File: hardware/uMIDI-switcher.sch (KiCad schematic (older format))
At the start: 23 parts, among them U1 MC7809CD, U2 MC7809CD, U3 MC7809CD, U4 MC7809CD, X1 CONN_01X02, X14 uMIDI GPIO3, X16 uMIDI Power, X2 CONN_01X02, X3 CONN_01X02, X4 CONN_01X02

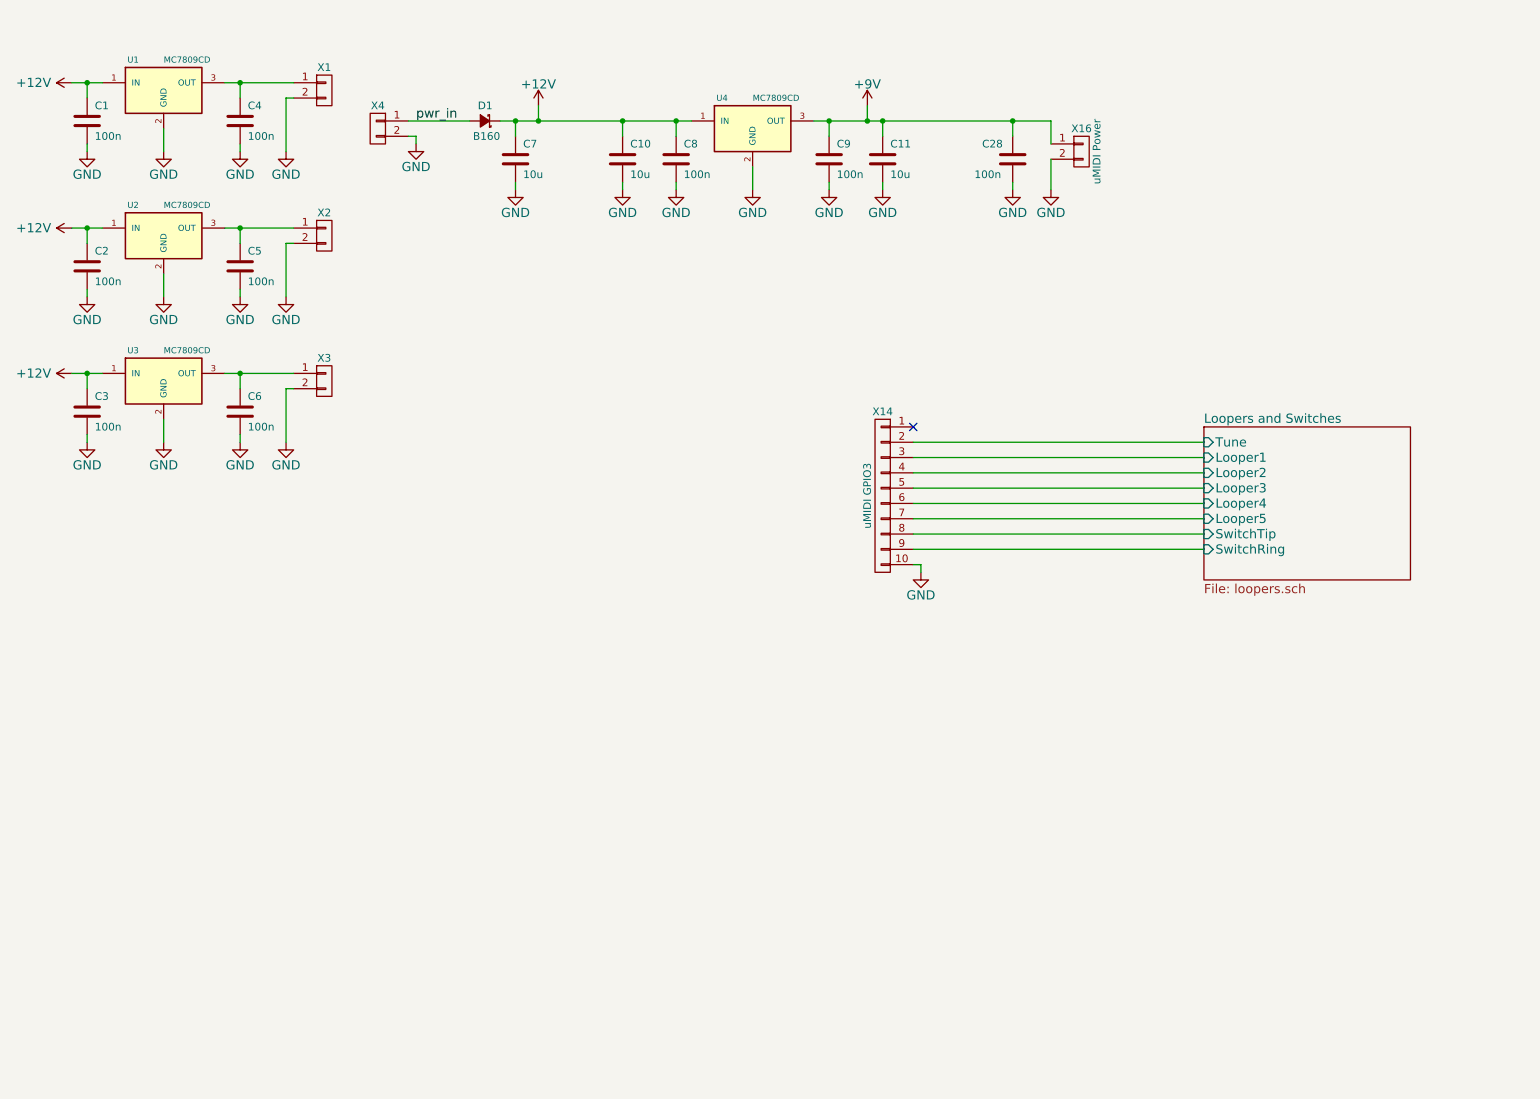
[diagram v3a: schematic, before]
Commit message: Integrate sheet looper.sch into top level sheet
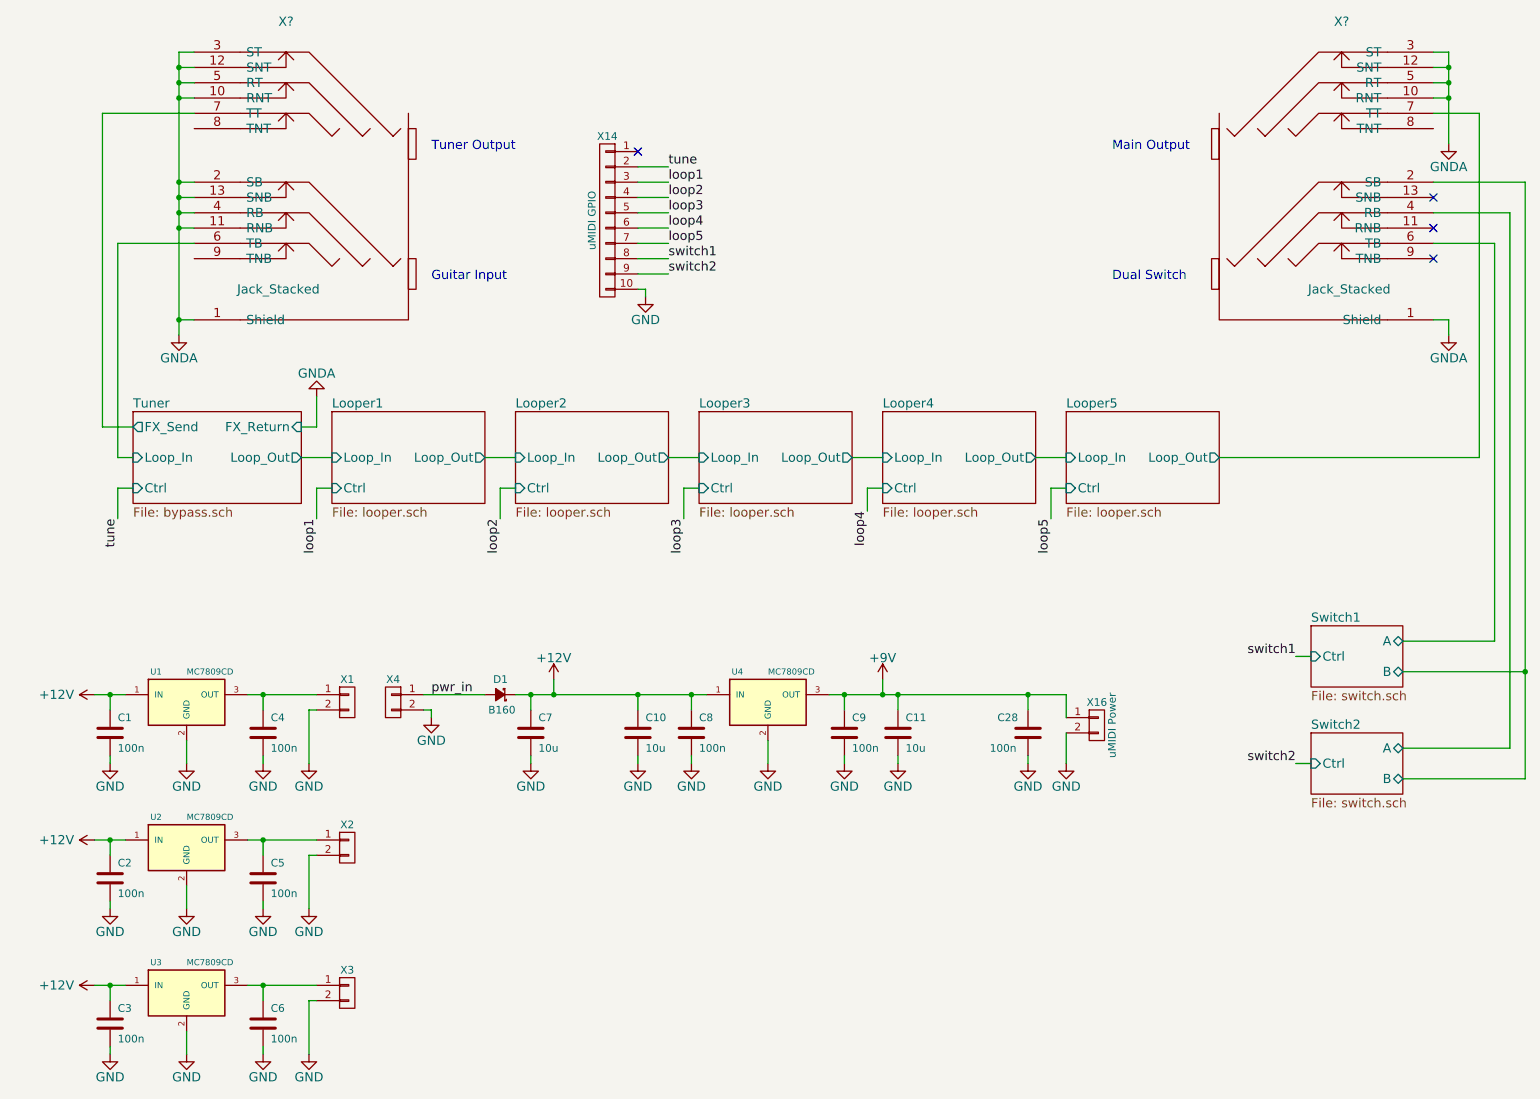
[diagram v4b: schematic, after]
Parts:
- added X? (x2): Jack_Stacked, uMIDI-switcher:NSJ12HF-1, symbol Jack_Stacked
- X14: value uMIDI GPIO3 -> uMIDI GPIO
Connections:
- net Loopers and Switches/Looper1 renamed loop1
- net Loopers and Switches/Looper2 renamed loop2
- net Loopers and Switches/Looper3 renamed loop3
- net Loopers and Switches/Looper4 renamed loop4
- net Loopers and Switches/Looper5 renamed loop5
- net Loopers and Switches/SwitchRing renamed switch2
- net Loopers and Switches/SwitchTip renamed switch1
- net Loopers and Switches/Tune renamed tune
- new net GNDA: X?.1 (Shield), X?.1 (Shield), X?.10 (RNT), X?.10 (RNT), X?.11 (RNB), X?.12 (SNT), X?.12 (SNT), X?.13 (SNB), X?.2 (SB), X?.3 (ST), X?.3 (ST), X?.4 (RB), X?.5 (RT), X?.5 (RT)
- new net Looper5/Loop_Out: X?.7 (TT)
- new net Switch1/A: X?.6 (TB)
- new net Switch1/B: X?.2 (SB)
- new net Switch2/A: X?.4 (RB)
- new net Tuner/FX_Send: X?.7 (TT)
- new net Tuner/Loop_In: X?.6 (TB)
- no-connect marks 1 -> 4
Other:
- note added: "Dual Switch"
- note added: "Guitar Input"
- note added: "Main Output"
- note added: "Tuner Output"
- moved on the sheet: C1, C10, C11, C2, C28, C3, C4, C5, C6, C7, C8, C9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

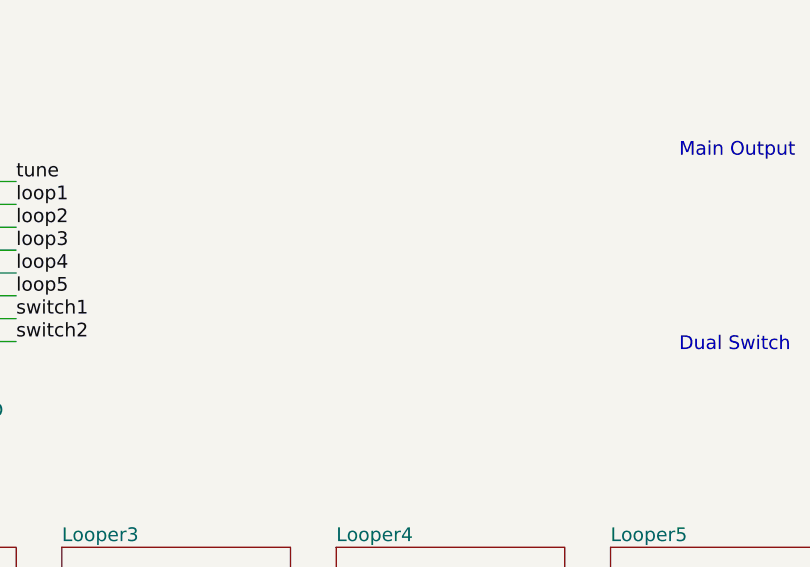
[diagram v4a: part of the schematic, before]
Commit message: Add optional gnd-gnda resistor
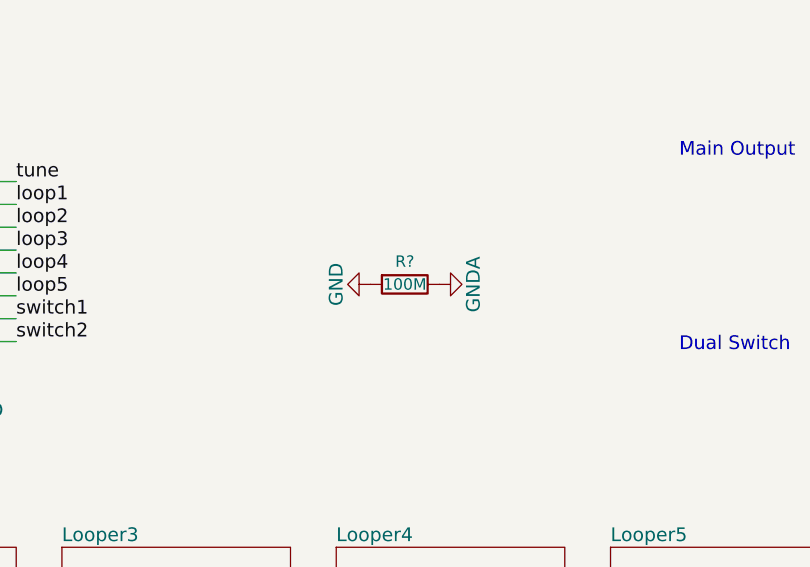
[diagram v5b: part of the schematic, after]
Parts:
- added R?: 100M, Resistors_SMD:R_0603, symbol R
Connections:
- net GND: now also R?.2
- net GNDA: now also R?.1
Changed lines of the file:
@@
 Wire Wire Line
 	4550 2300 4750 2300
+$Comp
+L GNDA #PWR?
+U 1 1 56216618
+P 6600 2050
+F 0 "#PWR?" H 6600 1800 60  0001 C CNN
+F 1 "GNDA" H 6600 1900 60  0000 C CNN
+F 2 "" H 6600 2050 60  0000 C CNN
+F 3 "" H 6600 2050 60  0000 C CNN
+	1    6600 2050
+	0    -1   -1   0
+$EndComp
+$Comp
+L GND #PWR?
+U 1 1 5621670A
+P 6300 2050
+F 0 "#PWR?" H 6300 1800 60  0001 C CNN
+F 1 "GND" H 6300 1900 60  0000 C CNN
+F 2 "" H 6300 2050 60  0000 C CNN
+F 3 "" H 6300 2050 60  0000 C CNN
+	1    6300 2050
+	0    1    1    0
+$EndComp
+$Comp
+L R R?
+U 1 1 56216FAF
+P 6450 2050
+F 0 "R?" V 6350 2050 50  0000 C CNN
+F 1 "100M" V 6450 2050 50  0000 C CNN
+F 2 "Resistors_SMD:R_0603" V 6380 2050 30  0001 C CNN
+F 3 "" H 6450 2050 30  0000 C CNN
+	1    6450 2050
+	0    1    1    0
+$EndComp
 $EndSCHEMATC

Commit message: Annotate
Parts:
- gave numbers to parts that had none: 3
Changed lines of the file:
@@
 $EndDescr
 $Comp
-L GND #PWR01
+L GND #PWR22
 U 1 1 54FA36B3
 P 4600 2450
-F 0 "#PWR01" H 4600 2200 60  0001 C CNN
+F 0 "#PWR22" H 4600 2200 60  0001 C CNN
 F 1 "GND" H 4600 2300 60  0000 C CNN
 F 2 "" H 4600 2450 60  0000 C CNN
@@
 NoConn ~ 4550 1500
 $Comp
-L +9V #PWR02
+L +9V #PWR26
 U 1 1 55B6A63F
 P 6150 4950
-F 0 "#PWR02" H 6150 4800 60  0001 C CNN
+F 0 "#PWR26" H 6150 4800 60  0001 C CNN
 F 1 "+9V" H 6150 5090 60  0000 C CNN
 F 2 "" H 6150 4950 60  0000 C CNN
@@
 $EndComp
 $Comp
-L +12V #PWR03
+L +12V #PWR20
 U 1 1 55B6C913
 P 4000 4950
-F 0 "#PWR03" H 4000 4800 60  0001 C CNN
+F 0 "#PWR20" H 4000 4800 60  0001 C CNN
 F 1 "+12V" H 4000 5090 60  0000 C CNN
 F 2 "" H 4000 4950 60  0000 C CNN
@@
 $EndComp
 $Comp
-L GND #PWR04
+L GND #PWR25
 U 1 1 55B70DFA
 P 5900 5500
-F 0 "#PWR04" H 5900 5250 60  0001 C CNN
+F 0 "#PWR25" H 5900 5250 60  0001 C CNN
 F 1 "GND" H 5900 5350 60  0000 C CNN
 F 2 "" H 5900 5500 60  0000 C CNN
@@
 $EndComp
 $Comp
-L GND #PWR05
+L GND #PWR23
 U 1 1 55B70E89
 P 4900 5500
-F 0 "#PWR05" H 4900 5250 60  0001 C CNN
+F 0 "#PWR23" H 4900 5250 60  0001 C CNN
 F 1 "GND" H 4900 5350 60  0000 C CNN
 F 2 "" H 4900 5500 60  0000 C CNN
@@
 $EndComp
 $Comp
-L GND #PWR06
+L GND #PWR24
 U 1 1 55B70EF4
 P 5400 5500
-F 0 "#PWR06" H 5400 5250 60  0001 C CNN
+F 0 "#PWR24" H 5400 5250 60  0001 C CNN
 F 1 "GND" H 5400 5350 60  0000 C CNN
 F 2 "" H 5400 5500 60  0000 C CNN
@@
 $EndComp
 $Comp
-L +12V #PWR07
+L +12V #PWR1
 U 1 1 55B757BE
 P 1000 5050
-F 0 "#PWR07" H 1000 4900 60  0001 C CNN
+F 0 "#PWR1" H 1000 4900 60  0001 C CNN
 F 1 "+12V" V 1000 5300 60  0000 C CNN
 F 2 "" H 1000 5050 60  0000 C CNN
@@
 $EndComp
 $Comp
-L GND #PWR08
+L GND #PWR11
 U 1 1 55B757D6
 P 2100 5500
-F 0 "#PWR08" H 2100 5250 60  0001 C CNN
+F 0 "#PWR11" H 2100 5250 60  0001 C CNN
 F 1 "GND" H 2100 5350 60  0000 C CNN
 F 2 "" H 2100 5500 60  0000 C CNN
@@
 $EndComp
 $Comp
-L GND #PWR09
+L GND #PWR4
 U 1 1 55B757DC
 P 1100 5500
-F 0 "#PWR09" H 1100 5250 60  0001 C CNN
+F 0 "#PWR4" H 1100 5250 60  0001 C CNN
 F 1 "GND" H 1100 5350 60  0000 C CNN
 F 2 "" H 1100 5500 60  0000 C CNN
@@
 $EndComp
 $Comp
-L GND #PWR010
+L GND #PWR8
 U 1 1 55B757E2
 P 1600 5500
-F 0 "#PWR010" H 1600 5250 60  0001 C CNN
+F 0 "#PWR8" H 1600 5250 60  0001 C CNN
 F 1 "GND" H 1600 5350 60  0000 C CNN
 F 2 "" H 1600 5500 60  0000 C CNN
@@
 $EndComp
 $Comp
-L GND #PWR011
+L GND #PWR14
 U 1 1 55B757FA
 P 2400 5500
-F 0 "#PWR011" H 2400 5250 60  0001 C CNN
+F 0 "#PWR14" H 2400 5250 60  0001 C CNN
 F 1 "GND" H 2400 5350 60  0000 C CNN
 F 2 "" H 2400 5500 60  0000 C CNN
@@
 $EndComp
 $Comp
-L GND #PWR012
+L GND #PWR18
 U 1 1 55B7738A
 P 3200 5200
-F 0 "#PWR012" H 3200 4950 60  0001 C CNN
+F 0 "#PWR18" H 3200 4950 60  0001 C CNN
 F 1 "GND" H 3200 5050 60  0000 C CNN
 F 2 "" H 3200 5200 60  0000 C CNN
@@
 $EndComp
 $Comp
-L GND #PWR013
+L GND #PWR19
 U 1 1 55B7845A
 P 3850 5500
-F 0 "#PWR013" H 3850 5250 60  0001 C CNN
+F 0 "#PWR19" H 3850 5250 60  0001 C CNN
 F 1 "GND" H 3850 5350 60  0000 C CNN
 F 2 "" H 3850 5500 60  0000 C CNN
@@
 $EndComp
 $Comp
-L +12V #PWR014
+L +12V #PWR2
 U 1 1 55F43672
 P 1000 6000
-F 0 "#PWR014" H 1000 5850 60  0001 C CNN
+F 0 "#PWR2" H 1000 5850 60  0001 C CNN
 F 1 "+12V" V 1000 6250 60  0000 C CNN
 F 2 "" H 1000 6000 60  0000 C CNN
@@
 $EndComp
 $Comp
-L GND #PWR015
+L GND #PWR12
 U 1 1 55F4368A
 P 2100 6450
-F 0 "#PWR015" H 2100 6200 60  0001 C CNN
+F 0 "#PWR12" H 2100 6200 60  0001 C CNN
 F 1 "GND" H 2100 6300 60  0000 C CNN
 F 2 "" H 2100 6450 60  0000 C CNN
@@
 $EndComp
 $Comp
-L GND #PWR016
+L GND #PWR5
 U 1 1 55F43690
 P 1100 6450
-F 0 "#PWR016" H 1100 6200 60  0001 C CNN
+F 0 "#PWR5" H 1100 6200 60  0001 C CNN
 F 1 "GND" H 1100 6300 60  0000 C CNN
 F 2 "" H 1100 6450 60  0000 C CNN
@@
 $EndComp
 $Comp
-L GND #PWR017
+L GND #PWR9
 U 1 1 55F43696
 P 1600 6450
-F 0 "#PWR017" H 1600 6200 60  0001 C CNN
+F 0 "#PWR9" H 1600 6200 60  0001 C CNN
 F 1 "GND" H 1600 6300 60  0000 C CNN
 F 2 "" H 1600 6450 60  0000 C CNN
@@
 $EndComp
 $Comp
-L GND #PWR018
+L GND #PWR15
 U 1 1 55F436AA
 P 2400 6450
-F 0 "#PWR018" H 2400 6200 60  0001 C CNN
+F 0 "#PWR15" H 2400 6200 60  0001 C CNN
 F 1 "GND" H 2400 6300 60  0000 C CNN
 F 2 "" H 2400 6450 60  0000 C CNN
@@
 $EndComp
 $Comp
-L +12V #PWR019
+L +12V #PWR3
 U 1 1 55F4379F
 P 1000 6950
-F 0 "#PWR019" H 1000 6800 60  0001 C CNN
+F 0 "#PWR3" H 1000 6800 60  0001 C CNN
 F 1 "+12V" V 1000 7200 60  0000 C CNN
 F 2 "" H 1000 6950 60  0000 C CNN
@@
 $EndComp
 $Comp
-L GND #PWR020
+L GND #PWR13
 U 1 1 55F437B7
 P 2100 7400
-F 0 "#PWR020" H 2100 7150 60  0001 C CNN
+F 0 "#PWR13" H 2100 7150 60  0001 C CNN
 F 1 "GND" H 2100 7250 60  0000 C CNN
 F 2 "" H 2100 7400 60  0000 C CNN
@@
 $EndComp
 $Comp
-L GND #PWR021
+L GND #PWR6
 U 1 1 55F437BD
 P 1100 7400
-F 0 "#PWR021" H 1100 7150 60  0001 C CNN
+F 0 "#PWR6" H 1100 7150 60  0001 C CNN
 F 1 "GND" H 1100 7250 60  0000 C CNN
 F 2 "" H 1100 7400 60  0000 C CNN
@@
 $EndComp
 $Comp
-L GND #PWR022
+L GND #PWR10
 U 1 1 55F437C3
 P 1600 7400
-F 0 "#PWR022" H 1600 7150 60  0001 C CNN
+F 0 "#PWR10" H 1600 7150 60  0001 C CNN
 F 1 "GND" H 1600 7250 60  0000 C CNN
 F 2 "" H 1600 7400 60  0000 C CNN
@@
 $EndComp
 $Comp
-L GND #PWR023
+L GND #PWR16
 U 1 1 55F437D7
 P 2400 7400
-F 0 "#PWR023" H 2400 7150 60  0001 C CNN
+F 0 "#PWR16" H 2400 7150 60  0001 C CNN
 F 1 "GND" H 2400 7250 60  0000 C CNN
 F 2 "" H 2400 7400 60  0000 C CNN
@@
 $EndComp
 $Comp
-L GND #PWR024
+L GND #PWR30
 U 1 1 55FDF929
 P 7100 5500
-F 0 "#PWR024" H 7100 5250 60  0001 C CNN
+F 0 "#PWR30" H 7100 5250 60  0001 C CNN
 F 1 "GND" H 7100 5350 60  0000 C CNN
 F 2 "" H 7100 5500 60  0000 C CNN
@@
 $EndComp
 $Comp
-L GND #PWR025
+L GND #PWR31
 U 1 1 55FE932A
 P 7350 5500
-F 0 "#PWR025" H 7350 5250 60  0001 C CNN
+F 0 "#PWR31" H 7350 5250 60  0001 C CNN
 F 1 "GND" H 7350 5350 60  0000 C CNN
 F 2 "" H 7350 5500 60  0000 C CNN
@@
 Connection ~ 6250 5050
 $Comp
-L GND #PWR026
+L GND #PWR27
 U 1 1 55FED47B
 P 6250 5500
-F 0 "#PWR026" H 6250 5250 60  0001 C CNN
+F 0 "#PWR27" H 6250 5250 60  0001 C CNN
 F 1 "GND" H 6250 5350 60  0000 C CNN
 F 2 "" H 6250 5500 60  0000 C CNN
@@
 	6250 5500 6250 5450
 $Comp
-L GND #PWR027
+L GND #PWR21
 U 1 1 55FED76E
 P 4550 5500
-F 0 "#PWR027" H 4550 5250 60  0001 C CNN
+F 0 "#PWR21" H 4550 5250 60  0001 C CNN
 F 1 "GND" H 4550 5350 60  0000 C CNN
 F 2 "" H 4550 5500 60  0000 C CNN
@@
 $EndSheet
 $Comp
-L Jack_Stacked X?
+L Jack_Stacked X5
 U 1 1 56223AA2
 P 3100 2650
-F 0 "X?" H 2250 4650 60  0000 C CNN
+F 0 "X5" H 2250 4650 60  0000 C CNN
 F 1 "Jack_Stacked" H 2200 2900 60  0000 C CNN
 F 2 "uMIDI-switcher:NSJ12HF-1" H 3100 2650 60  0001 C CNN
@@
 	1150 2100 1650 2100
 $Comp
-L GNDA #PWR?
+L GNDA #PWR17
 U 1 1 56223AAC
 P 2450 3100
-F 0 "#PWR?" H 2450 2850 60  0001 C CNN
+F 0 "#PWR17" H 2450 2850 60  0001 C CNN
 F 1 "GNDA" H 2450 2950 60  0000 C CNN
 F 2 "" H 2450 3100 60  0000 C CNN
@@
 	2450 3300 2350 3300
 $Comp
-L GNDA #PWR?
+L GNDA #PWR7
 U 1 1 56223AB3
 P 1550 2700
-F 0 "#PWR?" H 1550 2450 60  0001 C CNN
+F 0 "#PWR7" H 1550 2450 60  0001 C CNN
 F 1 "GNDA" H 1550 2550 60  0000 C CNN
 F 2 "" H 1550 2700 60  0000 C CNN
@@
 Connection ~ 1550 2000
 $Comp
-L Jack_Stacked X?
+L Jack_Stacked X6
 U 1 1 56223ACE
 P 8300 2650
-F 0 "X?" H 7450 4650 60  0000 C CNN
+F 0 "X6" H 7450 4650 60  0000 C CNN
 F 1 "Jack_Stacked" H 7400 2900 60  0000 C CNN
 F 2 "uMIDI-switcher:NSJ12HF-1" H 8300 2650 60  0001 C CNN
@@
 $EndComp
 $Comp
-L GNDA #PWR?
+L GNDA #PWR33
 U 1 1 56223AD5
 P 9850 2700
-F 0 "#PWR?" H 9850 2450 60  0001 C CNN
+F 0 "#PWR33" H 9850 2450 60  0001 C CNN
 F 1 "GNDA" H 9850 2550 60  0000 C CNN
 F 2 "" H 9850 2700 60  0000 C CNN
@@
 	10050 1250 9750 1250
 $Comp
-L GNDA #PWR?
+L GNDA #PWR32
 U 1 1 56223AE6
 P 9850 1450
-F 0 "#PWR?" H 9850 1200 60  0001 C CNN
+F 0 "#PWR32" H 9850 1200 60  0001 C CNN
 F 1 "GNDA" H 9850 1300 60  0000 C CNN
 F 2 "" H 9850 1450 60  0000 C CNN
@@
 	4550 2300 4750 2300
 $Comp
-L GNDA #PWR?
+L GNDA #PWR29
 U 1 1 56216618
 P 6600 2050
-F 0 "#PWR?" H 6600 1800 60  0001 C CNN
+F 0 "#PWR29" H 6600 1800 60  0001 C CNN
 F 1 "GNDA" H 6600 1900 60  0000 C CNN
 F 2 "" H 6600 2050 60  0000 C CNN
@@
 $EndComp
 $Comp
-L GND #PWR?
+L GND #PWR28
 U 1 1 5621670A
 P 6300 2050
-F 0 "#PWR?" H 6300 1800 60  0001 C CNN
+F 0 "#PWR28" H 6300 1800 60  0001 C CNN
 F 1 "GND" H 6300 1900 60  0000 C CNN
 F 2 "" H 6300 2050 60  0000 C CNN
@@
 $EndComp
 $Comp
-L R R?
+L R R1
 U 1 1 56216FAF
 P 6450 2050
-F 0 "R?" V 6350 2050 50  0000 C CNN
+F 0 "R1" V 6350 2050 50  0000 C CNN
 F 1 "100M" V 6450 2050 50  0000 C CNN
 F 2 "Resistors_SMD:R_0603" V 6380 2050 30  0001 C CNN

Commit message: Change D1 supplier
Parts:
- D1: Manufacturer (none) -> Diodes Incorporated; Manufacturer Part Number (none) -> B160-13-F; Part Number B160-FDICT-ND -> 621-B160-F; Supplier Digikey -> Mouser
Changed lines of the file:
@@
 F 1 "B160" H 3550 5150 50  0000 L CNN
 F 2 "Diodes_SMD:SMA_Standard" V 3650 5050 60  0001 C CNN
-F 3 "" V 3650 5050 60  0000 C CNN
-F 4 "Digikey" H 3650 5050 60  0001 C CNN "Supplier"
-F 5 "B160-FDICT-ND" H 3650 5050 60  0001 C CNN "Part Number"
+F 3 "http://www.mouser.com/ds/2/115/ds13002-60388.pdf" V 3650 5050 60  0001 C CNN
+F 4 "Mouser" H 3650 5050 60  0001 C CNN "Supplier"
+F 5 "621-B160-F" H 3650 5050 60  0001 C CNN "Part Number"
+F 6 "Diodes Incorporated" H 3650 5050 60  0001 C CNN "Manufacturer"
+F 7 "B160-13-F" H 3650 5050 60  0001 C CNN "Manufacturer Part Number"
 	1    3650 5050
 	-1   0    0    1

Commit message: Unify part fields
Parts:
- C1, C10, C11, C2, C28, C3, C4, C5, C6, C7, C8, C9, R1, X1, X14, X16, X2, X3, X4: Supplier (none) -> Mouser
- X5, X6: Link http://www.mouser.de/ProductDetail/Neutrik/NSJ12HF-1/?qs=%2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 -> (none)
